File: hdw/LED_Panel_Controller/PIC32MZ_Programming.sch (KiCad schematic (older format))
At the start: 13 parts, among them J801 PICKIT4, Q801 BSS214NW, SW801 MRST

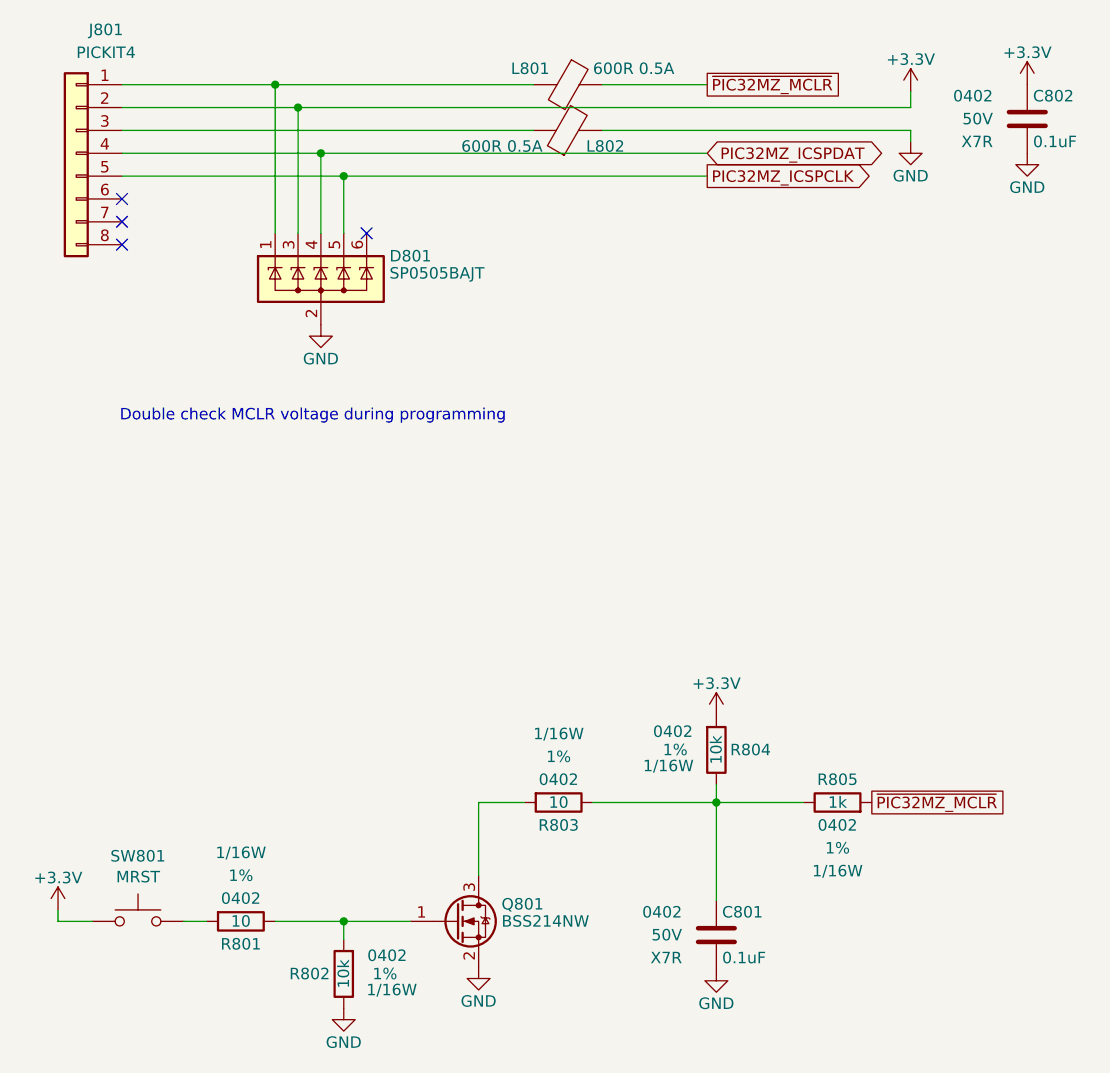
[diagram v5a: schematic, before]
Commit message: fixed SPI flash pull resistors, more PCB placement
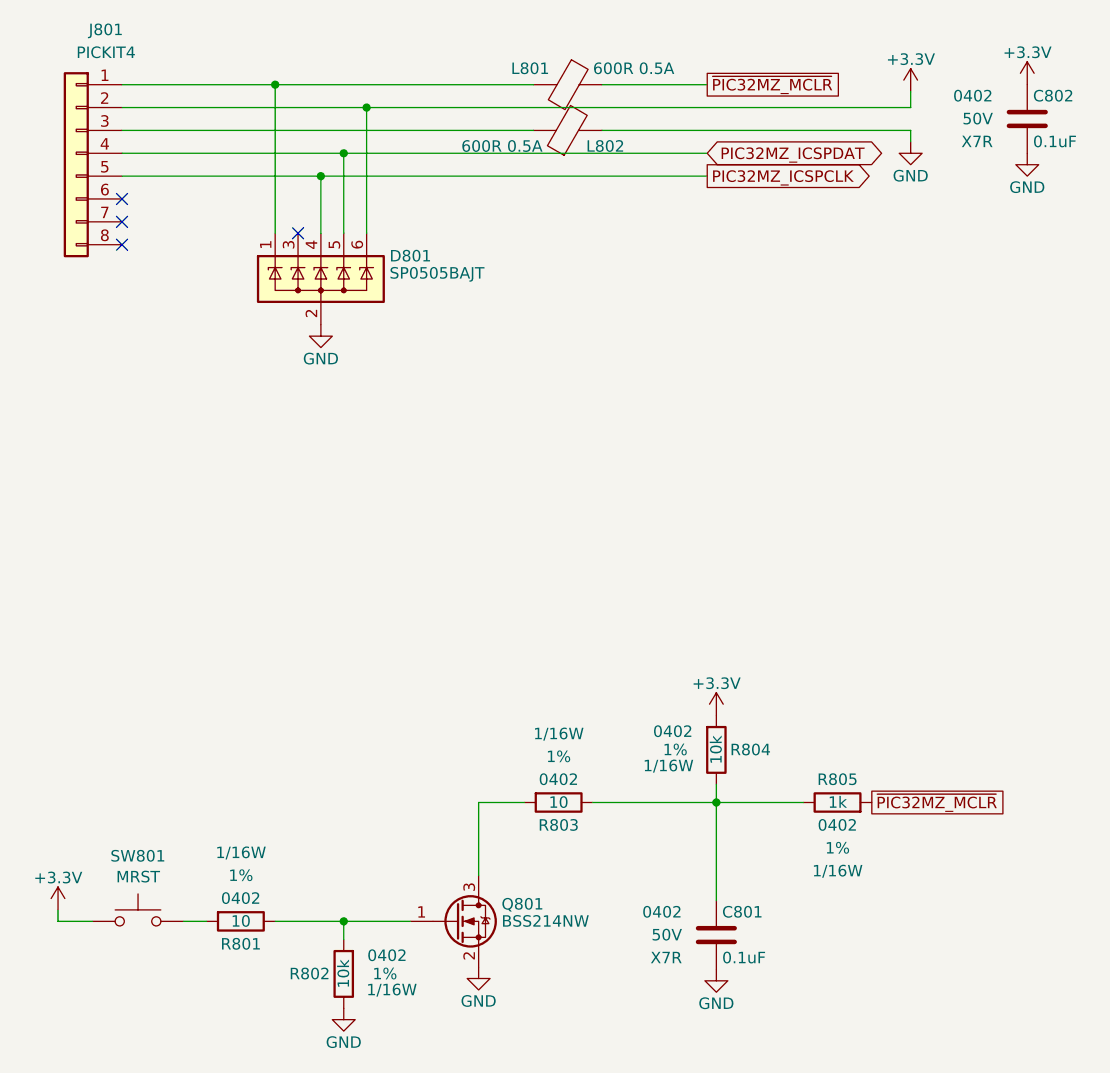
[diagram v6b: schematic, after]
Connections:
- net +3V3: now also D801.6 (K); no longer D801.3 (K)
- net PIC32MZ_ICSPCLK: now also D801.4 (K); no longer D801.5 (K)
- net PIC32MZ_ICSPDAT: now also D801.5 (K); no longer D801.4 (K)
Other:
- note removed: "Double check MCLR voltage during programming"
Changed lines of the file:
@@
 	0    -1   -1   0
-$EndComp
-Wire Wire Line
-	3170 2160 4040 2160
-Wire Wire Line
-	3170 2260 4140 2260
-$Comp
-L Power_Protection:SP0505BAJT D?
-U 1 1 6067D672
-P 4040 2710
-AR Path="/5F583BFC/6067D672" Ref="D?"  Part="1"
-AR Path="/5F5829A6/6067D672" Ref="D801"  Part="1"
-F 0 "D801" H 4340 2810 50  0000 L CNN
-F 1 "SP0505BAJT" H 4340 2735 50  0000 L CNN
-F 2 "TO_SOT_Packages_SMD:SOT-363_SC-70-6" H 4340 2660 50  0001 L CNN
-F 3 "http://www.littelfuse.com/~/media/files/littelfuse/technical%20resources/documents/data%20sheets/sp05xxba.pdf" H 4165 2835 50  0001 C CNN
-F 4 "F3160CT-ND" H 4040 2710 50  0001 C CNN "Digi-Key PN"
-	1    4040 2710
-	1    0    0    -1
 $EndComp
 $Comp
@@
 	3170 1860 3840 1860
 Wire Wire Line
-	3170 1960 3940 1960
-Wire Wire Line
-	3940 2510 3940 1960
-Connection ~ 3940 1960
-Wire Wire Line
-	3940 1960 6620 1960
-Wire Wire Line
-	4040 2510 4040 2160
-Connection ~ 4040 2160
-Wire Wire Line
-	4040 2160 5730 2160
-Wire Wire Line
-	4140 2510 4140 2260
-Connection ~ 4140 2260
-Wire Wire Line
-	4140 2260 5730 2260
-Wire Wire Line
 	3840 2510 3840 1860
 Connection ~ 3840 1860
 Wire Wire Line
 	3840 1860 4970 1860
-NoConn ~ 4240 2510
-Text Notes 3160 3340 0    50   ~ 0
-Double check MCLR voltage during programming
+Wire Wire Line
+	3170 1960 4240 1960
+Wire Wire Line
+	3170 2160 4140 2160
+Wire Wire Line
+	3170 2260 4040 2260
+Wire Wire Line
+	4240 2510 4240 1960
+Connection ~ 4240 1960
+Wire Wire Line
+	4240 1960 6620 1960
+$Comp
+L Power_Protection:SP0505BAJT D?
+U 1 1 6067D672
+P 4040 2710
+AR Path="/5F583BFC/6067D672" Ref="D?"  Part="1"
+AR Path="/5F5829A6/6067D672" Ref="D801"  Part="1"
+F 0 "D801" H 4340 2810 50  0000 L CNN
+F 1 "SP0505BAJT" H 4340 2735 50  0000 L CNN
+F 2 "TO_SOT_Packages_SMD:SOT-363_SC-70-6" H 4340 2660 50  0001 L CNN
+F 3 "http://www.littelfuse.com/~/media/files/littelfuse/technical%20resources/documents/data%20sheets/sp05xxba.pdf" H 4165 2835 50  0001 C CNN
+F 4 "F3160CT-ND" H 4040 2710 50  0001 C CNN "Digi-Key PN"
+	1    4040 2710
+	1    0    0    -1
+$EndComp
+Wire Wire Line
+	4140 2510 4140 2160
+Connection ~ 4140 2160
+Wire Wire Line
+	4140 2160 5730 2160
+Wire Wire Line
+	4040 2510 4040 2260
+Connection ~ 4040 2260
+Wire Wire Line
+	4040 2260 5730 2260
+NoConn ~ 3940 2510
 $EndSCHEMATC

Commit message: added BOMs, some consolidation
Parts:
- C801, C802: Digi-Key PN 490-10701-1-ND -> 490-10698-1-ND
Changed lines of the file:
@@
 F 5 "50V" H 6980 2010 50  0000 R CNN "Voltage"
 F 6 "X7R" H 6980 1910 50  0000 R CNN "Dielectric"
-F 7 "490-10701-1-ND" H 7555 2510 60  0001 C CNN "Digi-Key PN"
+F 7 "490-10698-1-ND" H 7555 2510 60  0001 C CNN "Digi-Key PN"
 	1    7130 2010
 	1    0    0    -1
@@
 F 5 "50V" H 5620 5580 50  0000 R CNN "Voltage"
 F 6 "X7R" H 5620 5480 50  0000 R CNN "Dielectric"
-F 7 "490-10701-1-ND" H 6195 6080 60  0001 C CNN "Digi-Key PN"
+F 7 "490-10698-1-ND" H 6195 6080 60  0001 C CNN "Digi-Key PN"
 	1    5770 5580
 	1    0    0    -1
